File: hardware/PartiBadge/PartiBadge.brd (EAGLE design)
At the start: 101.6 x 101.6 mm, 25 parts, among them J1 I2C, J2 Supply

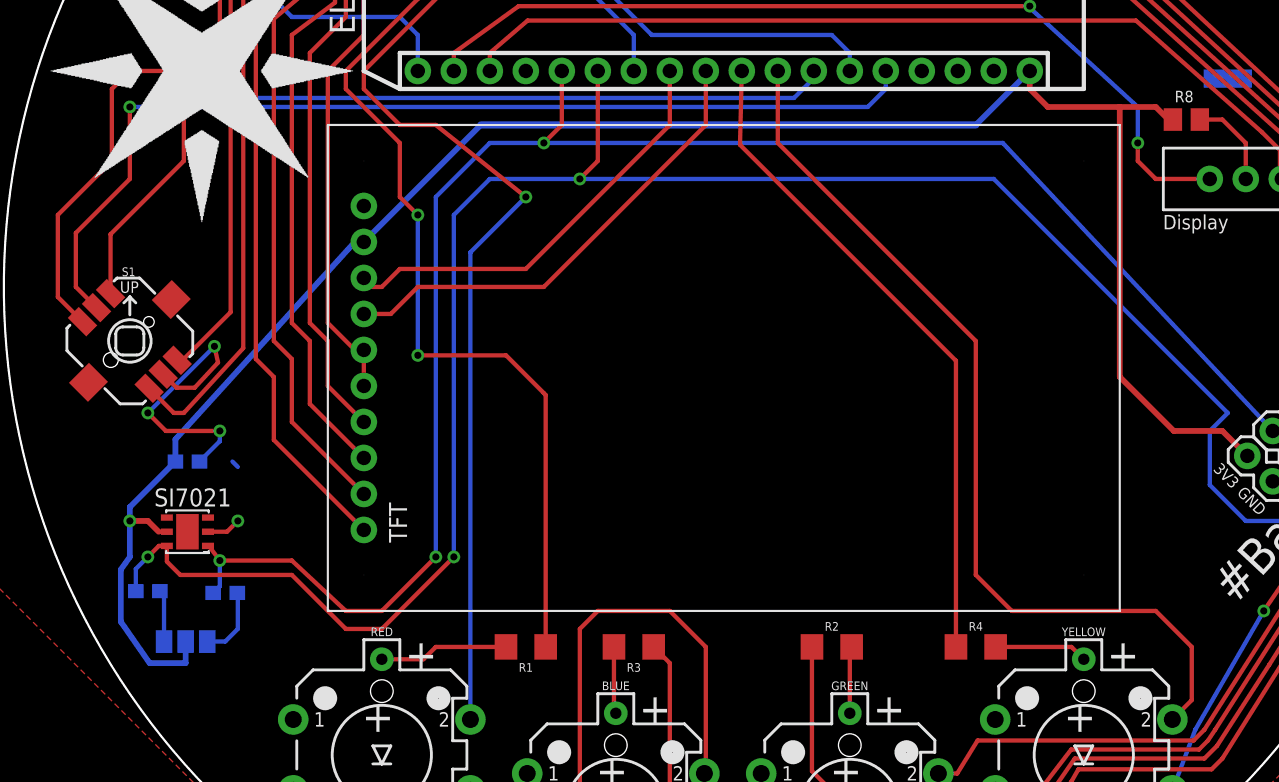
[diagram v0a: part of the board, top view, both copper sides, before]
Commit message: smash ref designators and clean up refs; closes #14
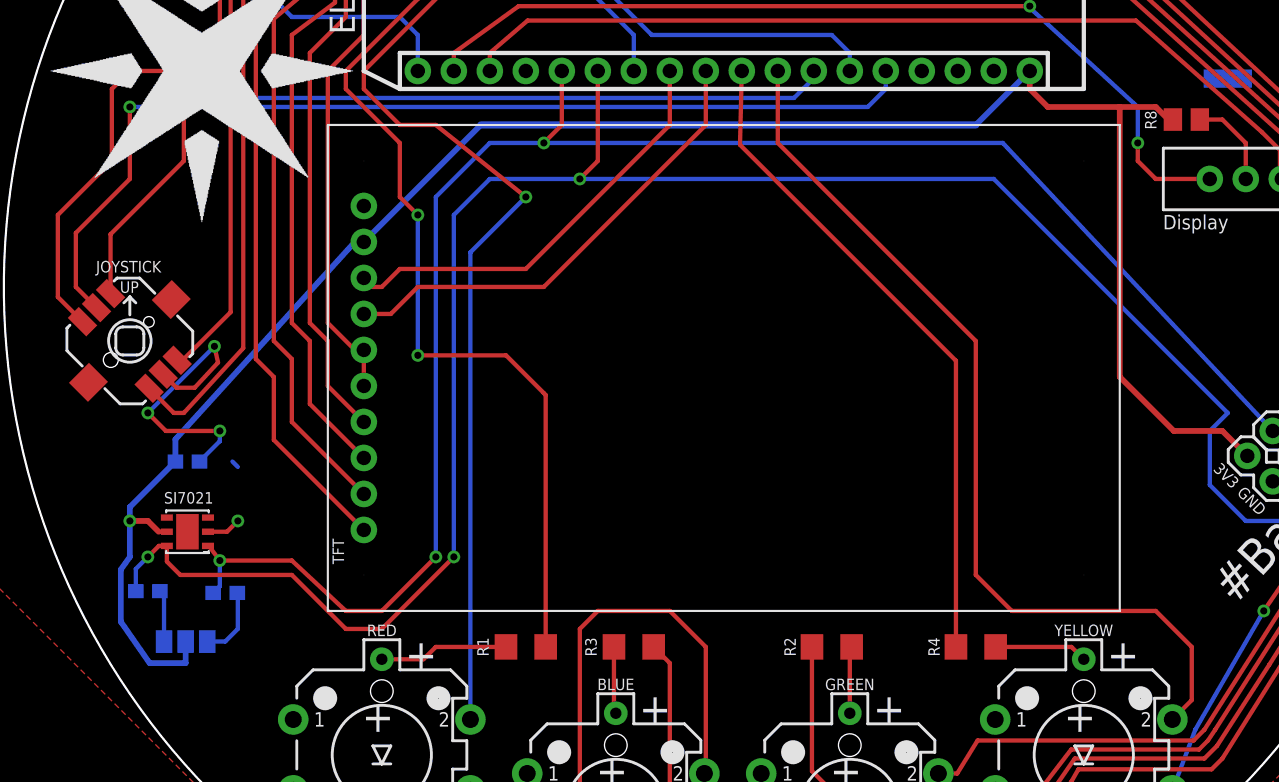
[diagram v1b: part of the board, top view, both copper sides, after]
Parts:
- renumbered S1 to JOYSTICK
